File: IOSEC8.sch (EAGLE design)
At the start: 27 parts

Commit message: Moved to metric grid for v2.0 release
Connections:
- net A0 renamed IO1
- net A1 renamed IO2
- net A2 renamed IO3
- net A3 renamed IO4
- net A4 renamed IO5
- net A5 renamed IO6
- net A6 renamed IO7
- net A7 renamed IO8
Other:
- moved on the sheet: J1, J2, J3, J4, J5, J6, J7, J8, JP1, LED2, R10, R11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

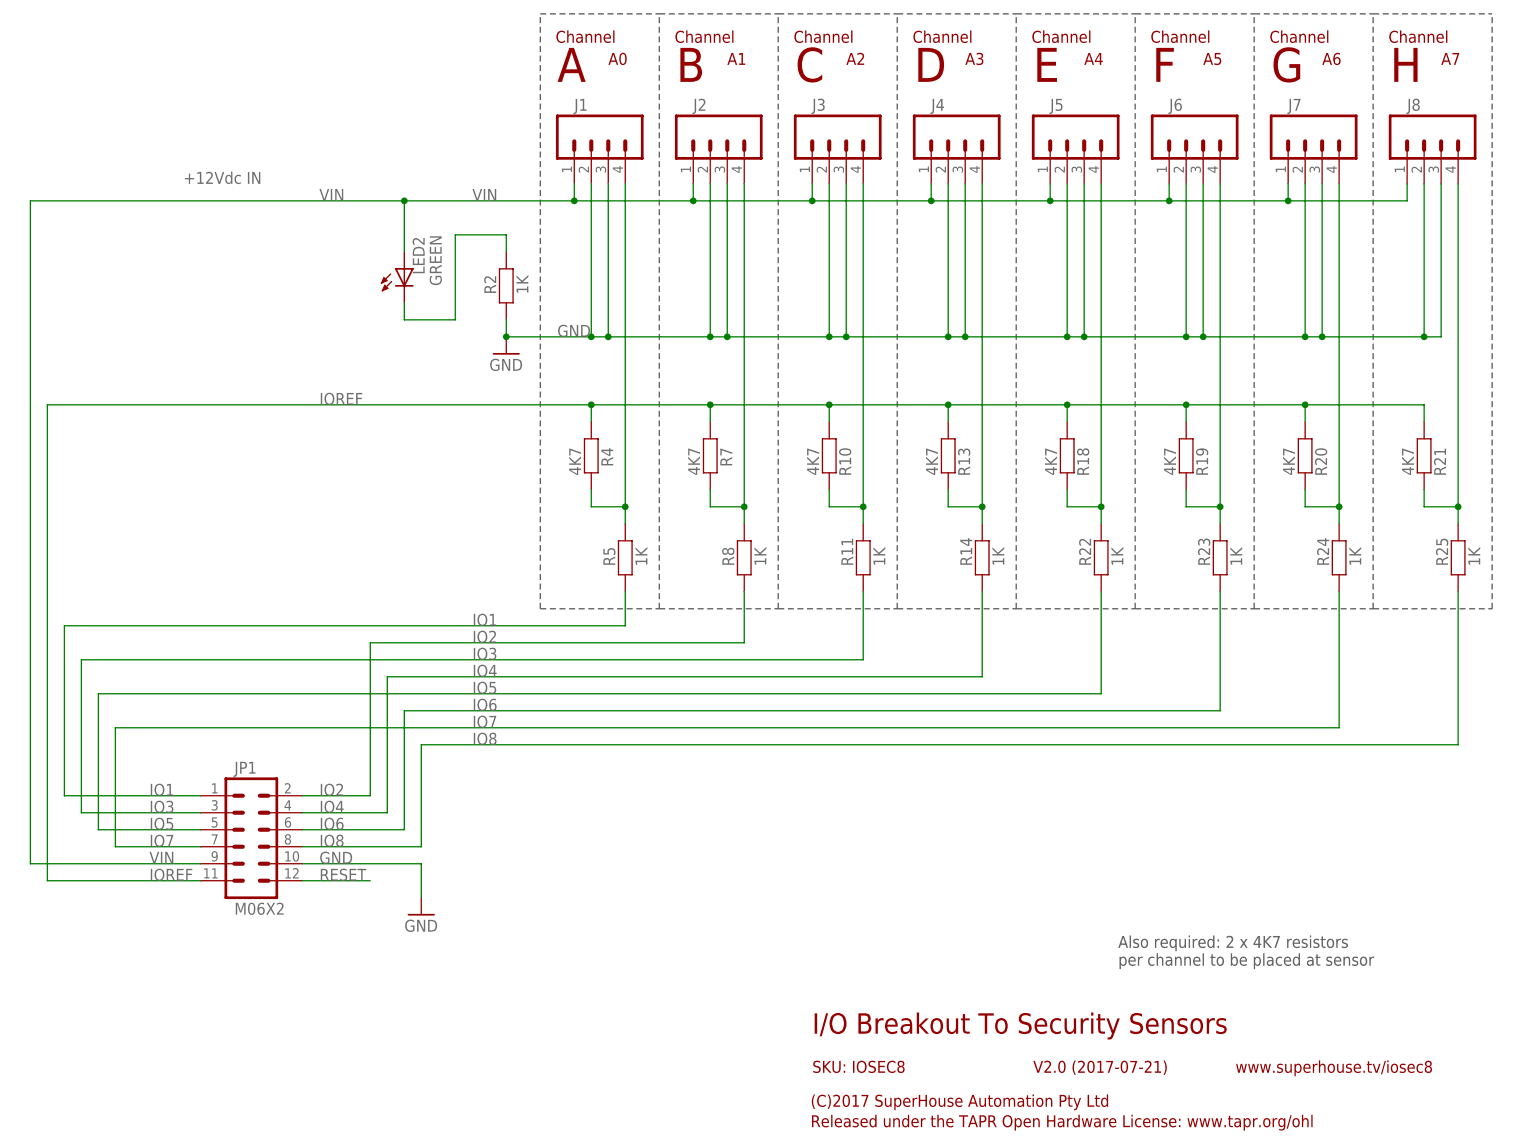
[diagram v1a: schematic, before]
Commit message: Added second IO port for status LEDs. Ready for v3.0 release
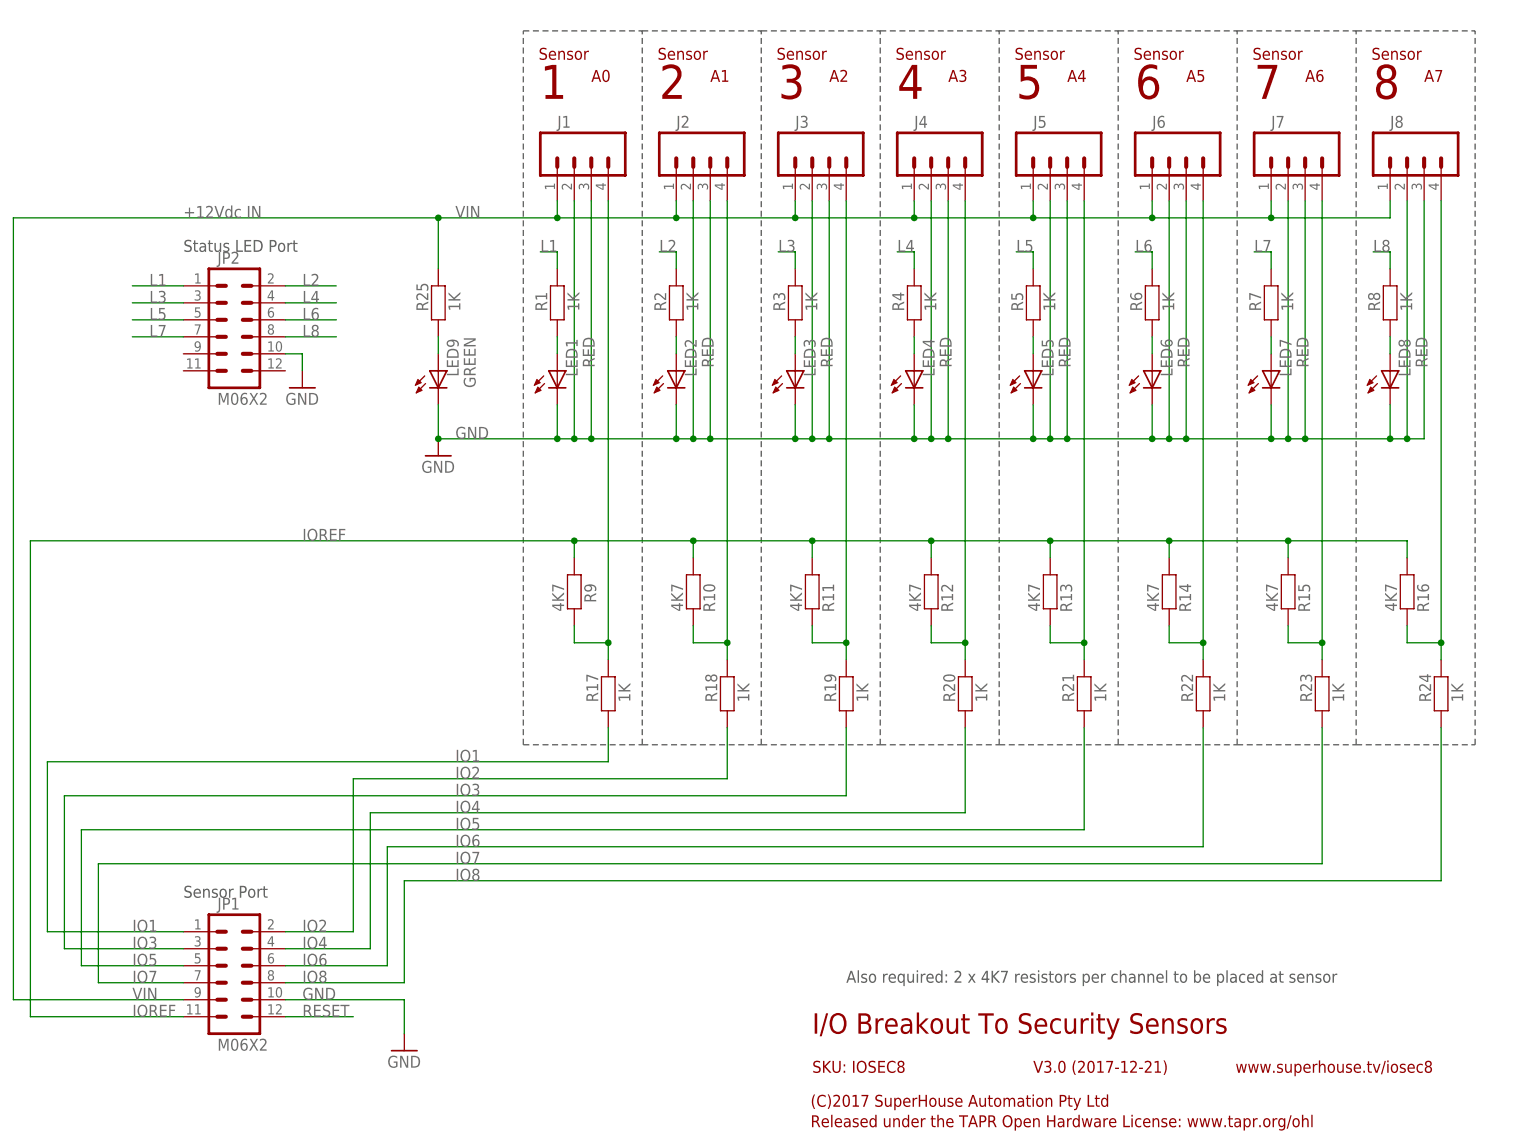
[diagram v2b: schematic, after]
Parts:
- added JP2: M06X2, freetronics-jon:M06X2
- added LED1, LED3, LED4, LED5, LED6, LED7, LED8: RED, freetronics-jon:LED0603
- added LED9: GREEN, freetronics-jon:LED0603
- added R1, R17, R3, R6: 1K, freetronics-jon:RESISTOR0603
- added R12, R15, R16, R9: 4K7, freetronics-jon:RESISTOR0603
- LED2: value GREEN -> RED
- R11, R14: value 1K -> 4K7
- R18, R19, R20, R21, R4, R7: value 4K7 -> 1K
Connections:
- new net L1: JP2.1, R1.2
- new net L2: JP2.2, R2.2
- new net L3: JP2.3, R3.2
- new net L4: JP2.4, R4.2
- new net L5: JP2.5, R5.2
- new net L6: JP2.6, R6.2
- new net L7: JP2.7, R7.2
- new net L8: JP2.8, R8.2
- new net N$16: LED2.A, R2.1
- new net N$17: LED3.A, R3.1
- new net N$18: LED4.A, R4.1
- new net N$19: LED5.A, R5.1
- new net N$2: LED1.A, R1.1
- new net N$20: LED6.A, R6.1
- new net N$21: LED7.A, R7.1
- new net N$22: LED8.A, R8.1
- net GND: now also JP2.10, LED1.C, LED2.C, LED3.C, LED4.C, LED5.C, LED6.C, LED7.C, LED8.C, LED9.C; no longer R2.1
- net IO1: now also R17.1; no longer R5.1
- net IO2: now also R18.1; no longer R8.1
- net IO3: now also R19.1; no longer R11.1
- net IO4: now also R20.1; no longer R14.1
- net IO5: now also R21.1; no longer R22.1
- net IO6: now also R22.1; no longer R23.1
- net IO7: now also R23.1; no longer R24.1
- net IO8: now also R24.1; no longer R25.1
- net IOREF: now also R11.1, R12.1, R14.1, R15.1, R16.1, R9.1; no longer R18.1, R19.1, R20.1, R21.1, R4.1, R7.1
- net N$1: now also LED9.A, R25.1; no longer LED2.C, R2.2
- net N$10: now also R16.2, R24.2; no longer R21.2, R25.2
- net N$249: now also R19.2; no longer R10.2
- net N$256: now also R12.2, R20.2; no longer R13.2, R14.2
- net N$262: now also R17.2, R9.2; no longer R4.2, R5.2
- net N$3: now also R10.2, R18.2; no longer R7.2, R8.2
- net N$7: now also R13.2, R21.2; no longer R18.2, R22.2
- net N$8: now also R14.2, R22.2; no longer R19.2, R23.2
- net N$9: now also R15.2, R23.2; no longer R20.2, R24.2
- net VIN: now also R25.2; no longer LED2.A
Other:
- note added: "1"
- note added: "2"
- note added: "3"
- note added: "4"
- note added: "5"
- note added: "6"
- note added: "7"
- note added: "8"
- note added: "Sensor"
- note added: "Sensor Port"
- note added: "Status LED Port"
- note added: "V3.0 (2017-12-21)"
- note removed: "A"
- note removed: "B"
- note removed: "C"
- note removed: "Channel"
- note removed: "D"
- note removed: "E"
- note removed: "F"
- note removed: "G"
- note removed: "H"
- note removed: "V2.0 (2017-07-21)"
- moved on the sheet: J1, J2, J3, J4, J5, J6, J7, J8, JP1, LED2, R10, R11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

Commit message: Massive update to reduce PCB size for v4.0 release
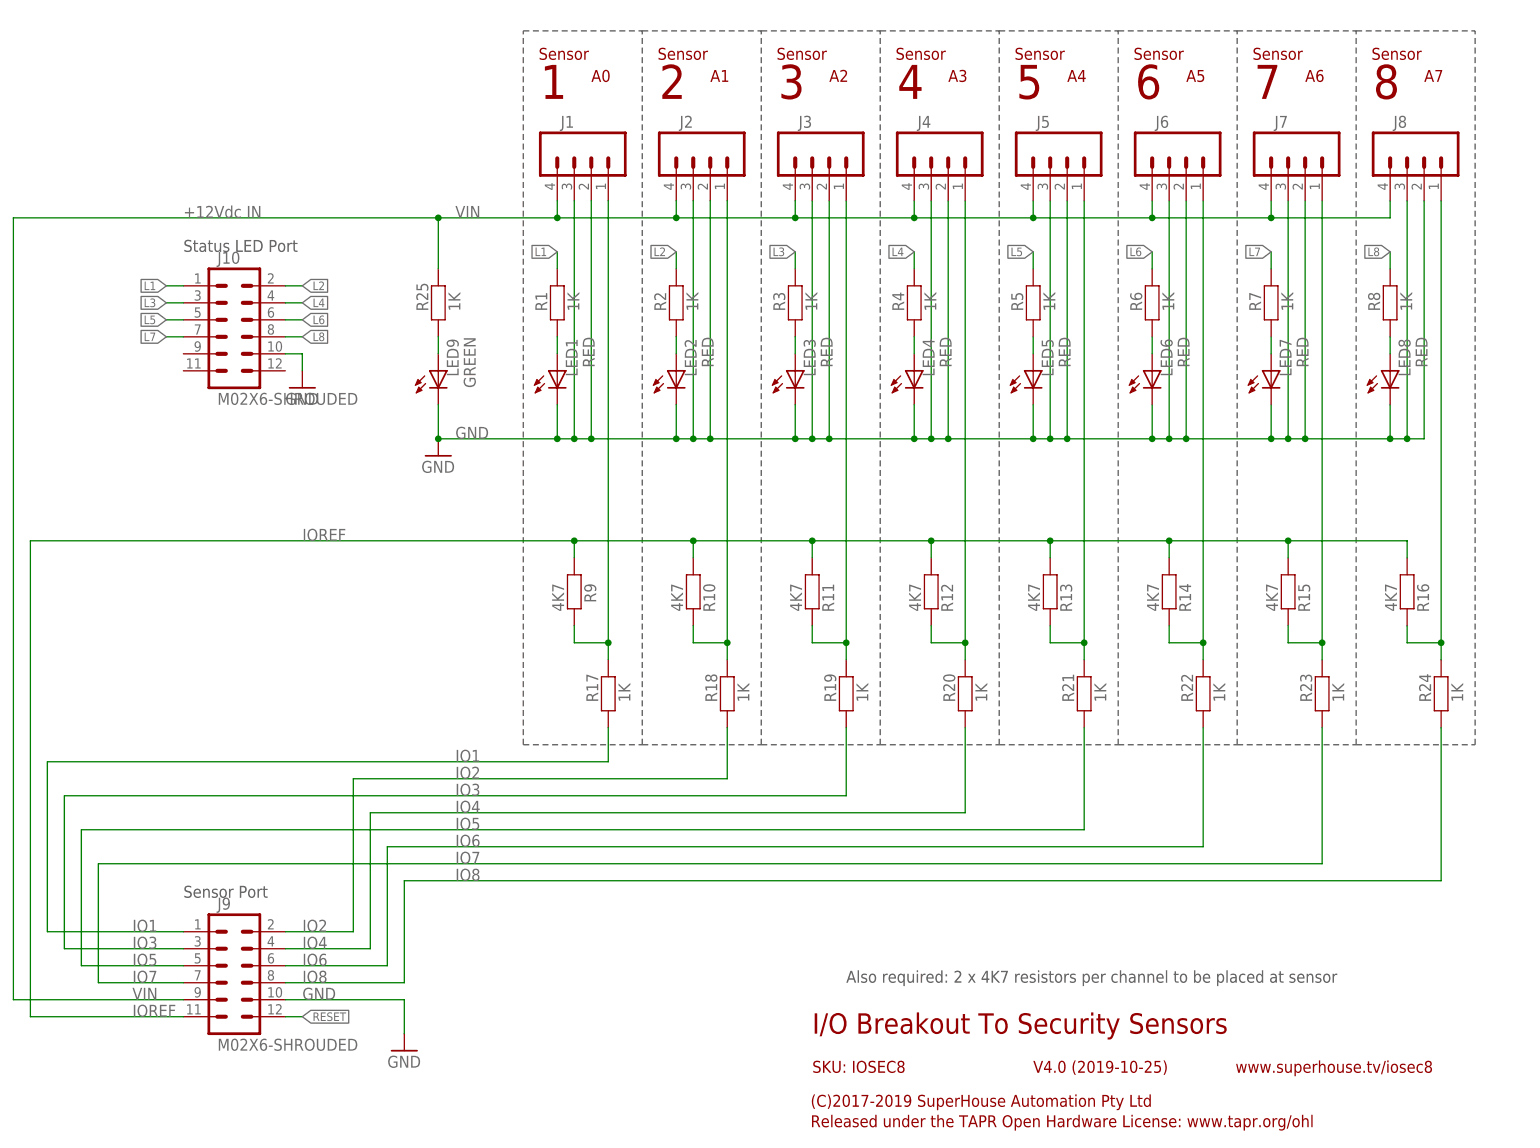
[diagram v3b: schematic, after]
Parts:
- removed JP1, JP2: M06X2, freetronics-jon:M06X2
- added J10, J9: M02X6-SHROUDED, SuperHouse-Connectors:M02X6-SHROUDED
- J1, J2, J3, J4, J5, J6, J7, J8: device freetronics-master-v1.1:M04SCREW -> SuperHouse-Connectors:M04-SCREW-3.5MM
- LED1, LED2, LED3, LED4, LED5, LED6, LED7, LED8, LED9: device freetronics-jon:LED0603 -> SuperHouse-LEDs:LED0603
- R1, R10, R11, R12, R13, R14, R15, R16, R17, R18, R19, R2, R20, R21, R22, R23, R24, R25, R3, R4, R5, R6, R7, R8, R9: device freetronics-jon:RESISTOR0603 -> SuperHouse-DiscreteSemi:RESISTOR0603
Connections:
- net GND: now also J10.10, J9.10; no longer JP1.10, JP2.10
- net IO1: now also J9.1; no longer JP1.1
- net IO2: now also J9.2; no longer JP1.2
- net IO3: now also J9.3; no longer JP1.3
- net IO4: now also J9.4; no longer JP1.4
- net IO5: now also J9.5; no longer JP1.5
- net IO6: now also J9.6; no longer JP1.6
- net IO7: now also J9.7; no longer JP1.7
- net IO8: now also J9.8; no longer JP1.8
- net IOREF: now also J9.11; no longer JP1.11
- net L1: now also J10.1; no longer JP2.1
- net L2: now also J10.2; no longer JP2.2
- net L3: now also J10.3; no longer JP2.3
- net L4: now also J10.4; no longer JP2.4
- net L5: now also J10.5; no longer JP2.5
- net L6: now also J10.6; no longer JP2.6
- net L7: now also J10.7; no longer JP2.7
- net L8: now also J10.8; no longer JP2.8
- net N$10: now also J8.1; no longer J8.4
- net N$249: now also J3.1; no longer J3.4
- net N$256: now also J4.1; no longer J4.4
- net N$262: now also J1.1; no longer J1.4
- net N$3: now also J2.1; no longer J2.4
- net N$7: now also J5.1; no longer J5.4
- net N$8: now also J6.1; no longer J6.4
- net N$9: now also J7.1; no longer J7.4
- net RESET: now also J9.12; no longer JP1.12
- net VIN: now also J1.4, J2.4, J3.4, J4.4, J5.4, J6.4, J7.4, J8.4, J9.9; no longer J1.1, J2.1, J3.1, J4.1, J5.1, J6.1, J7.1, J8.1, JP1.9
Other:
- note added: "(C)2017-2019 SuperHouse Automation Pty Ltd"
- note added: "V4.0 (2019-10-25)"
- note removed: "(C)2017 SuperHouse Automation Pty Ltd"
- note removed: "V3.0 (2017-12-21)"
